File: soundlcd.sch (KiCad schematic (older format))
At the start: 35 parts, among them J10 Speaker, J8 GPIO3, J9 Audio Out, SW3 UBTN1, SW4 UBTN2, U1 74HCT04, U13 AY-3-8910, U19 RTC72421, U20 ULN2803A, U21 74HC245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

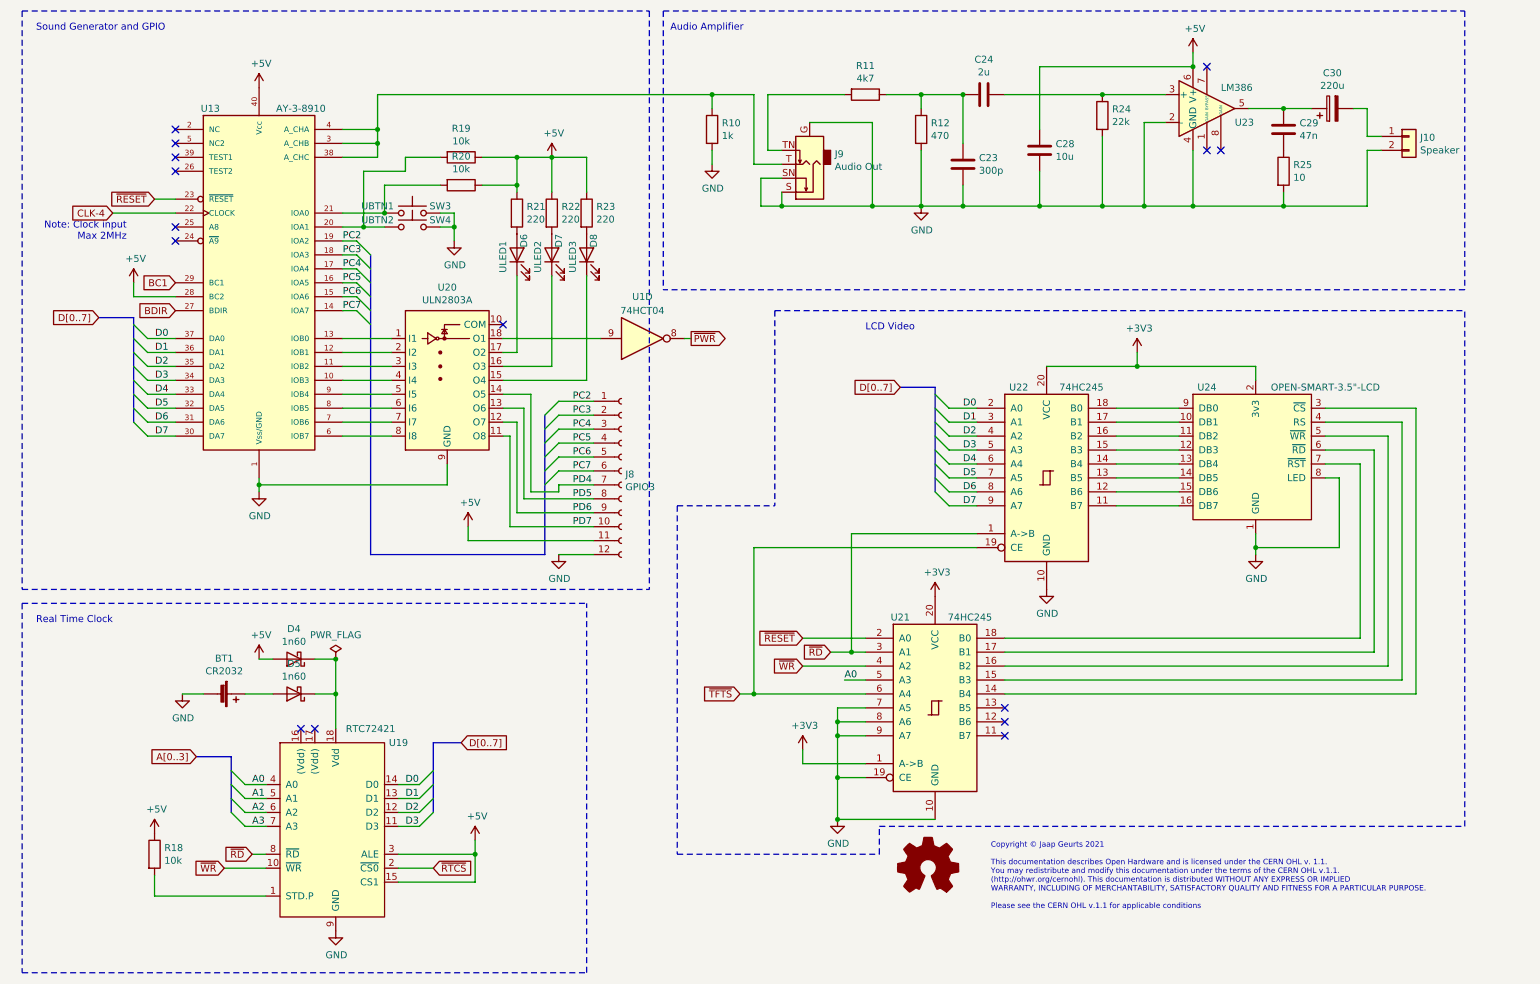
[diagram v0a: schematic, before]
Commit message: PCB tracing done
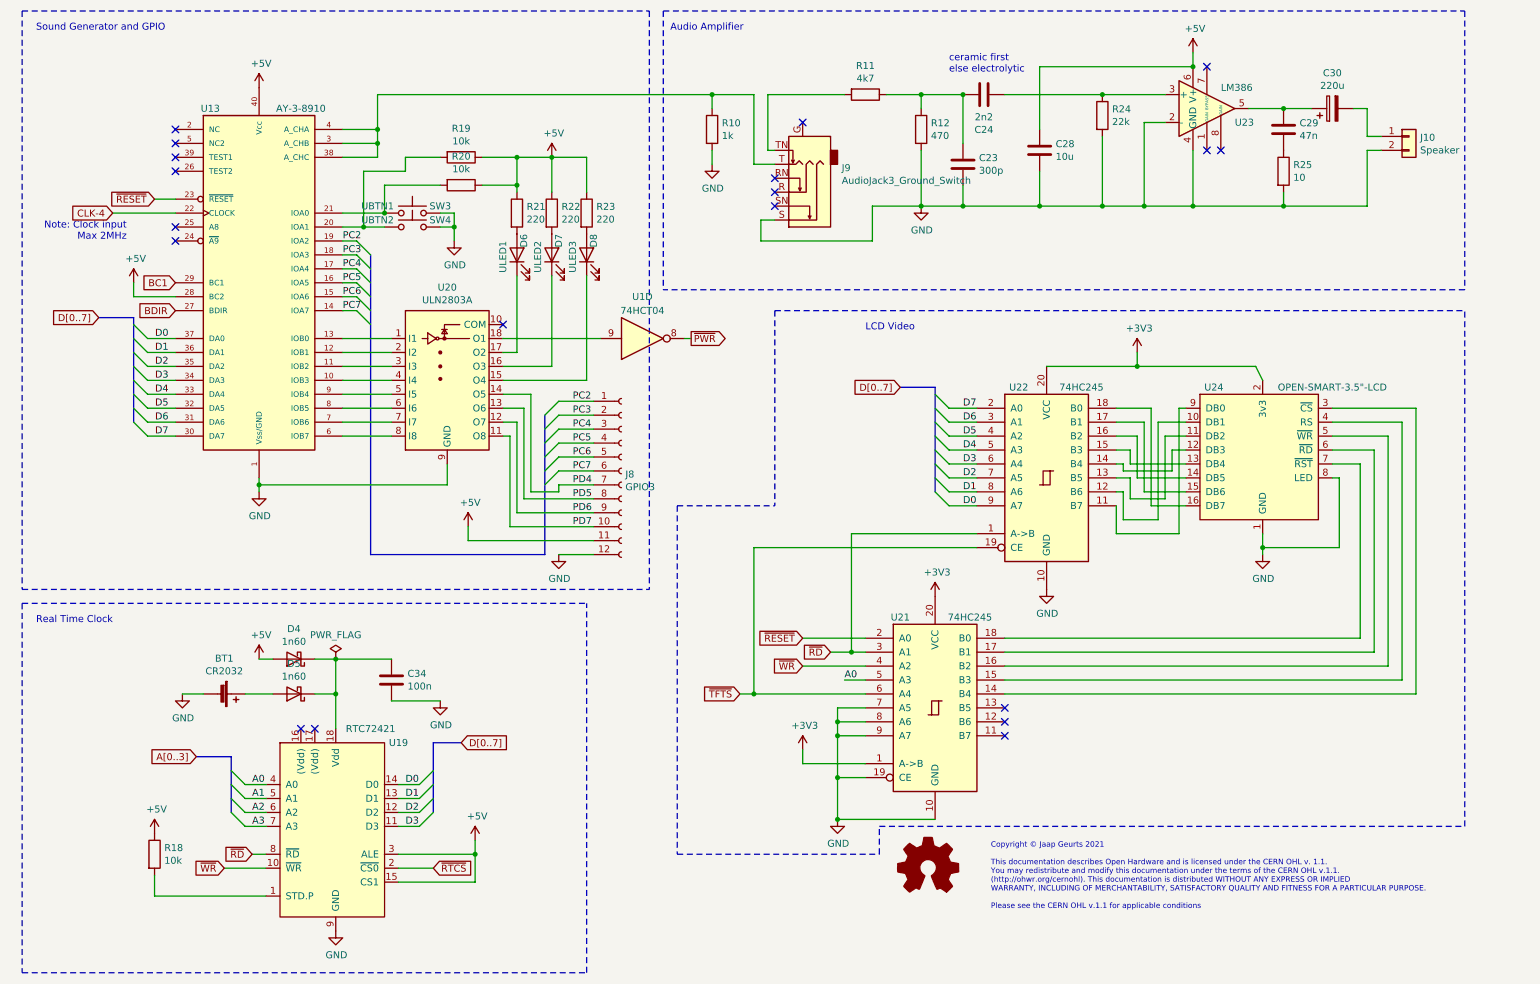
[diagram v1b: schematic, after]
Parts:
- removed J9: Audio Out, Connector_Audio:Jack_3.5mm_Ledino_KB3SPRS_Horizontal, symbol Connector:AudioJack2_Ground_Switch
- added C34: 100n, Capacitor_THT:C_Disc_D5.0mm_W2.5mm_P2.50mm, symbol Device:C
- added J9: AudioJack3_Ground_Switch, Connector_Audio:Jack_3.5mm_Ledino_KB3SPRS_Horizontal, symbol Connector:AudioJack3_Ground_Switch
- C24: value 2u -> 2n2
- U23: footprint Package_DIP:DIP-8-16_W7.62mm_Socket_LongPads -> Package_DIP:DIP-8_W7.62mm_Socket_LongPads
- U24: footprint Connector_PinSocket_2.54mm:PinSocket_1x16_P2.54mm_Vertical -> Personal:OPENSMART-3.5in-LCD
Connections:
- net D0: now also U22.9 (A7); no longer U22.2 (A0)
- net D1: now also U22.8 (A6); no longer U22.3 (A1)
- net D2: now also U22.7 (A5); no longer U22.4 (A2)
- net D3: now also U22.6 (A4); no longer U22.5 (A3)
- net D4: now also U22.5 (A3); no longer U22.6 (A4)
- net D5: now also U22.4 (A2); no longer U22.7 (A5)
- net D6: now also U22.3 (A1); no longer U22.8 (A6)
- net D7: now also U22.2 (A0); no longer U22.9 (A7)
- net GND: now also C34.2, J9.S
- net at R10.1, U13.3 (A_CHB), U13.38 (A_CHC)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: now also J9.T
- net at C23.1, R11.1, R12.1: now also C24.1; no longer C24.2
- net at R11.2: now also J9.TN
- net at R24.1, U23.3 (+): now also C24.2; no longer C24.1
- net at D4.1 (K), D5.1 (K), U19.18 (Vdd): now also C34.1
- net at U24.10 (DB1): now also U22.12 (B6); no longer U22.17 (B1)
- net at U24.11 (DB2): now also U22.13 (B5); no longer U22.16 (B2)
- net at U24.12 (DB3): now also U22.14 (B4); no longer U22.15 (B3)
- net at U24.13 (DB4): now also U22.15 (B3); no longer U22.14 (B4)
- net at U24.14 (DB5): now also U22.16 (B2); no longer U22.13 (B5)
- net at U24.15 (DB6): now also U22.17 (B1); no longer U22.12 (B6)
- net at U24.16 (DB7): now also U22.18 (B0); no longer U22.11 (B7)
- net at U24.9 (DB0): now also U22.11 (B7); no longer U22.18 (B0)
- no-connect marks 15 -> 19
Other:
- note added: "ceramic first\nelse electrolytic"
- moved on the sheet: U24
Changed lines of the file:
@@
 P 7650 1250
 F 0 "C24" V 7398 1250 50  0000 C CNN
-F 1 "2u" V 7489 1250 50  0000 C CNN
+F 1 "2n2" V 7489 1250 50  0000 C CNN
 F 2 "Capacitor_THT:CP_Radial_D5.0mm_P2.00mm" H 7688 1100 50  0001 C CNN
 F 3 "~" H 7650 1250 50  0001 C CNN
 	1    7650 1250
-	0    1    1    0
+	0    -1   -1   0
 $EndComp
 Wire Wire Line
@@
 Wire Wire Line
 	2850 5300 3000 5300
-Wire Wire Line
-	3000 5300 3000 5550
 Wire Wire Line
 	2850 5550 3000 5550
@@
 	3300 1500 3300 1250
 Connection ~ 3300 1500
-Connection ~ 7500 1250
 Text Notes 5400 800  0    50   ~ 0
 Audio Amplifier
@@
 F 0 "U23" H 9450 1250 50  0000 L CNN
 F 1 "LM386" H 9350 1500 50  0000 L CNN
-F 2 "Package_DIP:DIP-8-16_W7.62mm_Socket_LongPads" H 9350 1450 50  0001 C CNN
+F 2 "Package_DIP:DIP-8_W7.62mm_Socket_LongPads" H 9350 1450 50  0001 C CNN
 F 3 "http://www.ti.com/lit/ds/symlink/lm386.pdf" H 9450 1550 50  0001 C CNN
 	1    9250 1350
@@
 L personal:OPEN-SMART-3.5"-LCD U24
 U 1 1 6052728B
-P 9600 3850
-F 0 "U24" H 9250 4350 50  0000 C CNN
-F 1 "OPEN-SMART-3.5\"-LCD" H 10100 4350 50  0000 C CNN
-F 2 "Connector_PinSocket_2.54mm:PinSocket_1x16_P2.54mm_Vertical" H 9600 3450 50  0001 C CNN
-F 3 "" H 9600 3450 50  0001 C CNN
-	1    9600 3850
+P 9650 3850
+F 0 "U24" H 9300 4350 50  0000 C CNN
+F 1 "OPEN-SMART-3.5\"-LCD" H 10150 4350 50  0000 C CNN
+F 2 "Personal:OPENSMART-3.5in-LCD" H 9650 3450 50  0001 C CNN
+F 3 "" H 9650 3450 50  0001 C CNN
+	1    9650 3850
 	1    0    0    -1
 $EndComp
@@
 	1    0    0    -1
 $EndComp
-Wire Wire Line
-	8600 3500 9050 3500
-Wire Wire Line
-	8600 3600 9050 3600
-Wire Wire Line
-	8600 3700 9050 3700
-Wire Wire Line
-	8600 3800 9050 3800
-Wire Wire Line
-	8600 3900 9050 3900
-Wire Wire Line
-	8600 4000 9050 4000
-Wire Wire Line
-	8600 4100 9050 4100
-Wire Wire Line
-	8600 4200 9050 4200
 Wire Bus Line
 	7050 3350 7300 3350
@@
 Wire Wire Line
 	7400 4200 7600 4200
+Text Label 7500 4200 0    50   ~ 0
+D0
+Text Label 7500 4100 0    50   ~ 0
+D1
+Text Label 7500 4000 0    50   ~ 0
+D2
+Text Label 7500 3900 0    50   ~ 0
+D3
+Text Label 7500 3800 0    50   ~ 0
+D4
+Text Label 7500 3700 0    50   ~ 0
+D5
+Text Label 7500 3600 0    50   ~ 0
+D6
 Text Label 7500 3500 0    50   ~ 0
-D0
-Text Label 7500 3600 0    50   ~ 0
-D1
-Text Label 7500 3700 0    50   ~ 0
-D2
-Text Label 7500 3800 0    50   ~ 0
-D3
-Text Label 7500 3900 0    50   ~ 0
-D4
-Text Label 7500 4000 0    50   ~ 0
-D5
-Text Label 7500 4100 0    50   ~ 0
-D6
-Text Label 7500 4200 0    50   ~ 0
 D7
 $Comp
@@
 L power:GND #PWR0121
 U 1 1 6061C17D
-P 9600 4550
-F 0 "#PWR0121" H 9600 4300 50  0001 C CNN
-F 1 "GND" H 9605 4377 50  0000 C CNN
-F 2 "" H 9600 4550 50  0001 C CNN
-F 3 "" H 9600 4550 50  0001 C CNN
-	1    9600 4550
+P 9650 4550
+F 0 "#PWR0121" H 9650 4300 50  0001 C CNN
+F 1 "GND" H 9655 4377 50  0000 C CNN
+F 2 "" H 9650 4550 50  0001 C CNN
+F 3 "" H 9650 4550 50  0001 C CNN
+	1    9650 4550
 	1    0    0    -1
 $EndComp
@@
 	8750 3200 9600 3200
 Wire Wire Line
-	9600 3200 9600 3300
+	9600 3200 9650 3300
 Connection ~ 8750 3200
 $Comp
@@
 	6350 6050 6350 5950
 Wire Wire Line
-	9600 4400 9600 4500
-Wire Wire Line
-	9600 4500 10200 4500
-Wire Wire Line
-	10200 4500 10200 4000
-Wire Wire Line
-	10200 4000 10100 4000
-Connection ~ 9600 4500
-Wire Wire Line
-	9600 4500 9600 4550
-Wire Wire Line
-	10100 3900 10350 3900
-Wire Wire Line
-	10350 3900 10350 5150
+	9650 4400 9650 4500
+Connection ~ 9650 4500
+Wire Wire Line
+	9650 4500 9650 4550
 Wire Wire Line
 	10350 5150 7800 5150
@@
 	7800 5250 10450 5250
 Wire Wire Line
-	10450 5250 10450 3800
-Wire Wire Line
-	10450 3800 10100 3800
-Wire Wire Line
-	10100 3700 10550 3700
-Wire Wire Line
 	10550 3700 10550 5350
 Wire Wire Line
 	10550 5350 7800 5350
-Wire Wire Line
-	10100 3600 10650 3600
-Wire Wire Line
-	10650 3600 10650 5450
-Wire Wire Line
-	10650 5450 7800 5450
-Wire Wire Line
-	10100 3500 10750 3500
-Wire Wire Line
-	10750 3500 10750 5550
 NoConn ~ 7800 5650
 NoConn ~ 7800 5750
 NoConn ~ 7800 5850
-Text GLabel 5900 5550 0    50   Input ~ 0
-~TFTS
-Wire Wire Line
-	5900 5550 6000 5550
 Wire Wire Line
 	7800 5550 10750 5550
 Wire Wire Line
-	6000 4500 6000 5550
-Wire Wire Line
 	6000 4500 7600 4500
-Connection ~ 6000 5550
-Wire Wire Line
-	6000 5550 6800 5550
-Text GLabel 6350 5150 0    50   Input ~ 0
-~RESET
-Wire Wire Line
-	6650 5450 6800 5450
-Text GLabel 6550 5250 0    50   Input ~ 0
-~RD
-Wire Wire Line
-	6350 5150 6800 5150
-Wire Wire Line
-	6550 5250 6700 5250
-Text GLabel 6350 5350 0    50   Input ~ 0
-~WR
-Wire Wire Line
-	6350 5350 6800 5350
-Text Label 6650 5450 0    50   ~ 0
-A0
-Wire Wire Line
-	6700 5250 6700 4400
-Wire Wire Line
-	6700 4400 7600 4400
-Connection ~ 6700 5250
-Wire Wire Line
-	6700 5250 6800 5250
 Wire Notes Line
 	6150 2800 6150 4200
@@
 	6600 5650 6600 5750
 Connection ~ 6600 5750
-$Comp
-L Connector:AudioJack2_Ground_Switch J9
-U 1 1 606E3024
-P 6400 1750
-F 0 "J9" H 6220 1676 50  0000 R CNN
-F 1 "Audio Out" H 6220 1767 50  0000 R CNN
-F 2 "Connector_Audio:Jack_3.5mm_Ledino_KB3SPRS_Horizontal" H 6400 1950 50  0001 C CNN
-F 3 "~" H 6400 1950 50  0001 C CNN
-	1    6400 1750
+Wire Wire Line
+	6100 1250 6650 1250
+Wire Wire Line
+	6850 2050 7200 2050
+$Comp
+L Connector:AudioJack3_Ground_Switch J9
+U 1 1 607D6A8E
+P 6350 1950
+F 0 "J9" H 6070 1776 50  0000 R CNN
+F 1 "AudioJack3_Ground_Switch" H 6070 1867 50  0000 R CNN
+F 2 "Connector_Audio:Jack_3.5mm_Ledino_KB3SPRS_Horizontal" H 6350 1950 50  0001 C CNN
+F 3 "~" H 6350 1950 50  0001 C CNN
+	1    6350 1950
 	-1   0    0    1
 $EndComp
 Wire Wire Line
-	6100 1250 6650 1250
-Wire Wire Line
-	6200 1750 6000 1750
+	6150 1750 6000 1750
 Wire Wire Line
 	6000 1750 6000 1250
 Wire Wire Line
-	6200 1650 6100 1650
+	6150 1650 6100 1650
 Wire Wire Line
 	6100 1650 6100 1250
 Wire Wire Line
-	6200 1950 6200 2050
-Wire Wire Line
-	6200 2050 6850 2050
-Wire Wire Line
-	6200 1850 6050 1850
-Wire Wire Line
-	6050 1850 6050 2050
-Wire Wire Line
-	6050 2050 6200 2050
-Connection ~ 6200 2050
-Wire Wire Line
-	6400 1450 6850 1450
-Wire Wire Line
-	6850 1450 6850 2050
+	6050 2150 6150 2150
+Wire Wire Line
+	6050 2150 6050 2300
+Wire Wire Line
+	6050 2300 6850 2300
+Wire Wire Line
+	6850 2300 6850 2050
+NoConn ~ 6150 1850
+NoConn ~ 6150 1950
+NoConn ~ 6350 1450
+NoConn ~ 6150 2050
+Connection ~ 7500 1250
+Text Notes 7400 1100 0    50   ~ 0
+ceramic first\nelse electrolytic
+$Comp
+L Device:C C?
+U 1 1 609A93FD
+P 3400 5450
+AR Path="/609A93FD" Ref="C?"  Part="1"
+AR Path="/601FFB8A/609A93FD" Ref="C34"  Part="1"
+F 0 "C34" H 3515 5496 50  0000 L CNN
+F 1 "100n" H 3515 5405 50  0000 L CNN
+F 2 "Capacitor_THT:C_Disc_D5.0mm_W2.5mm_P2.50mm" H 3438 5300 50  0001 C CNN
+F 3 "~" H 3400 5450 50  0001 C CNN
+	1    3400 5450
+	1    0    0    -1
+$EndComp
+Wire Wire Line
+	3400 5300 3000 5300
+$Comp
+L power:GND #PWR014
+U 1 1 609C8B4D
+P 3750 5600
+F 0 "#PWR014" H 3750 5350 50  0001 C CNN
+F 1 "GND" H 3755 5427 50  0000 C CNN
+F 2 "" H 3750 5600 50  0001 C CNN
+F 3 "" H 3750 5600 50  0001 C CNN
+	1    3750 5600
+	1    0    0    -1
+$EndComp
+Wire Wire Line
+	3750 5600 3400 5600
+Wire Wire Line
+	3000 5300 3000 5550
+Wire Wire Line
+	8600 3500 8850 3500
+Wire Wire Line
+	8850 3500 8850 4200
+Wire Wire Line
+	8850 4200 9100 4200
+Wire Wire Line
+	8600 3600 8800 3600
+Wire Wire Line
+	8800 3600 8800 4100
+Wire Wire Line
+	8600 3700 8750 3700
+Wire Wire Line
+	8750 3700 8750 4000
+Wire Wire Line
+	8750 4000 9100 4000
+Wire Wire Line
+	8600 3800 8700 3800
+Wire Wire Line
+	8700 3800 8700 3900
+Wire Wire Line
+	8700 3900 9100 3900
+Wire Wire Line
+	8600 3900 8650 3900
+Wire Wire Line
+	8650 3900 8650 3950
+Wire Wire Line
+	8650 3950 9000 3950
+Wire Wire Line
+	9000 3950 9000 3800
+Wire Wire Line
+	9000 3800 9100 3800
+Wire Wire Line
+	8800 4100 9100 4100
+Wire Wire Line
+	8600 4000 8700 4000
+Wire Wire Line
+	8700 4000 8700 4150
+Wire Wire Line
+	8700 4150 8950 4150
+Wire Wire Line
+	8950 4150 8950 3700
+Wire Wire Line
+	8950 3700 9100 3700
+Wire Wire Line
+	8600 4100 8650 4100
+Wire Wire Line
+	8650 4100 8650 4300
+Wire Wire Line
+	8650 4300 8900 4300
+Wire Wire Line
+	8900 4300 8900 3600
+Wire Wire Line
+	8900 3600 9100 3600
+Wire Wire Line
+	6700 4400 7600 4400
+Wire Wire Line
+	6350 5350 6800 5350
+Text GLabel 6350 5350 0    50   Input ~ 0
+~WR
+Text Label 6650 5450 0    50   ~ 0
+A0
+Wire Wire Line
+	6650 5450 6800 5450
+Wire Wire Line
+	10650 5450 7800 5450
+Wire Wire Line
+	6700 5250 6800 5250
+Connection ~ 6700 5250
+Wire Wire Line
+	6700 5250 6700 4400
+Wire Wire Line
+	6550 5250 6700 5250
+Text GLabel 6550 5250 0    50   Input ~ 0
+~RD
+Wire Wire Line
+	6000 5550 6800 5550
+Connection ~ 6000 5550
+Wire Wire Line
+	6000 4500 6000 5550
+Wire Wire Line
+	5900 5550 6000 5550
+Text GLabel 5900 5550 0    50   Input ~ 0
+~TFTS
+Wire Wire Line
+	6350 5150 6800 5150
+Text GLabel 6350 5150 0    50   Input ~ 0
+~RESET
+Wire Wire Line
+	10750 3500 10750 5550
+Wire Wire Line
+	10650 3600 10650 5450
+Wire Wire Line
+	10450 5250 10450 3800
+Wire Wire Line
+	10350 3900 10350 5150
+Wire Wire Line
+	9650 4500 10200 4500
+Wire Wire Line
+	10200 4500 10200 4000
+Wire Wire Line
+	10200 4000 10150 4000
+Wire Wire Line
+	9100 3500 9050 3500
+Wire Wire Line
+	9050 3500 9050 4400
+Wire Wire Line
+	9050 4400 8600 4400
+Wire Wire Line
+	8600 4400 8600 4200
+Wire Bus Line
+	4500 3550 4500 4550
+Wire Bus Line
+	3250 2400 3250 4550
+Wire Bus Line
+	7300 3350 7300 4100
 Wire Bus Line
 	2250 6000 2250 6400
@@
 	3700 5900 3700 6400
 Wire Bus Line
-	3250 2400 3250 4550
-Wire Bus Line
-	4500 3550 4500 4550
-Wire Bus Line
-	7300 3350 7300 4100
-Wire Bus Line
 	1550 2850 1550 3600
-Connection ~ 6850 2050
-Wire Wire Line
-	6850 2050 7200 2050
+Wire Wire Line
+	10150 3500 10750 3500
+Wire Wire Line
+	10150 3600 10650 3600
+Wire Wire Line
+	10150 3700 10550 3700
+Wire Wire Line
+	10450 3800 10150 3800
+Wire Wire Line
+	10150 3900 10350 3900
 $EndSCHEMATC

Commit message: Fixed up issues
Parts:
- D6: value ULED1 -> LED 1
- D7: value ULED2 -> LED 2
- D8: value ULED3 -> LED 3
- J9: value AudioJack3_Ground_Switch -> Audio out
- SW3: value UBTN1 -> BTN 1
- SW4: value UBTN2 -> BTN 2
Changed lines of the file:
@@
 P 4300 2400
 F 0 "D6" H 4450 2350 50  0000 R CNN
-F 1 "ULED1" H 4400 2500 50  0000 R CNN
+F 1 "LED 1" H 4400 2500 50  0000 R CNN
 F 2 "LED_THT:LED_D5.0mm" H 4300 2400 50  0001 C CNN
 F 3 "~" H 4300 2400 50  0001 C CNN
@@
 P 4550 2400
 F 0 "D7" H 4700 2350 50  0000 R CNN
-F 1 "ULED2" H 4650 2500 50  0000 R CNN
+F 1 "LED 2" H 4650 2500 50  0000 R CNN
 F 2 "LED_THT:LED_D5.0mm" H 4550 2400 50  0001 C CNN
 F 3 "~" H 4550 2400 50  0001 C CNN
@@
 P 4800 2400
 F 0 "D8" H 4950 2350 50  0000 R CNN
-F 1 "ULED3" H 4900 2500 50  0000 R CNN
+F 1 "LED 3" H 4900 2500 50  0000 R CNN
 F 2 "LED_THT:LED_D5.0mm" H 4800 2400 50  0001 C CNN
 F 3 "~" H 4800 2400 50  0001 C CNN
@@
 P 3550 2100
 F 0 "SW3" H 3750 2150 50  0000 C CNN
-F 1 "UBTN1" H 3300 2150 50  0000 C CNN
+F 1 "BTN 1" H 3300 2150 50  0000 C CNN
 F 2 "Button_Switch_THT:SW_PUSH_6mm" H 3550 2300 50  0001 C CNN
 F 3 "~" H 3550 2300 50  0001 C CNN
@@
 P 3550 2200
 F 0 "SW4" H 3750 2250 50  0000 C CNN
-F 1 "UBTN2" H 3300 2250 50  0000 C CNN
+F 1 "BTN 2" H 3300 2250 50  0000 C CNN
 F 2 "Button_Switch_THT:SW_PUSH_6mm" H 3550 2400 50  0001 C CNN
 F 3 "~" H 3550 2400 50  0001 C CNN
@@
 P 6350 1950
 F 0 "J9" H 6070 1776 50  0000 R CNN
-F 1 "AudioJack3_Ground_Switch" H 6070 1867 50  0000 R CNN
+F 1 "Audio out" H 6070 1867 50  0000 R CNN
 F 2 "Connector_Audio:Jack_3.5mm_Ledino_KB3SPRS_Horizontal" H 6350 1950 50  0001 C CNN
 F 3 "~" H 6350 1950 50  0001 C CNN
@@
 Wire Wire Line
 	8600 4400 8600 4200
+Wire Wire Line
+	10150 3500 10750 3500
+Wire Wire Line
+	10150 3600 10650 3600
+Wire Wire Line
+	10150 3700 10550 3700
+Wire Wire Line
+	10450 3800 10150 3800
+Wire Wire Line
+	10150 3900 10350 3900
+Wire Bus Line
+	2250 6000 2250 6400
+Wire Bus Line
+	3700 5900 3700 6400
+Wire Bus Line
+	3250 2400 3250 4550
 Wire Bus Line
 	4500 3550 4500 4550
 Wire Bus Line
-	3250 2400 3250 4550
-Wire Bus Line
 	7300 3350 7300 4100
 Wire Bus Line
-	2250 6000 2250 6400
-Wire Bus Line
-	3700 5900 3700 6400
-Wire Bus Line
 	1550 2850 1550 3600
-Wire Wire Line
-	10150 3500 10750 3500
-Wire Wire Line
-	10150 3600 10650 3600
-Wire Wire Line
-	10150 3700 10550 3700
-Wire Wire Line
-	10450 3800 10150 3800
-Wire Wire Line
-	10150 3900 10350 3900
 $EndSCHEMATC
